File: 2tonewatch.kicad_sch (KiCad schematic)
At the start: 1 part, among them U1 STM32WB55CGUx

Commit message: added eink conn page
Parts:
- removed U1: STM32WB55CGUx, Package_DFN_QFN:QFN-48-1EP_7x7mm_P0.5mm_EP5.6x5.6mm, symbol MCU_ST_STM32WB:STM32WB55CGUx
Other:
- added sheet eink-connector (eink-connector.kicad_sch)

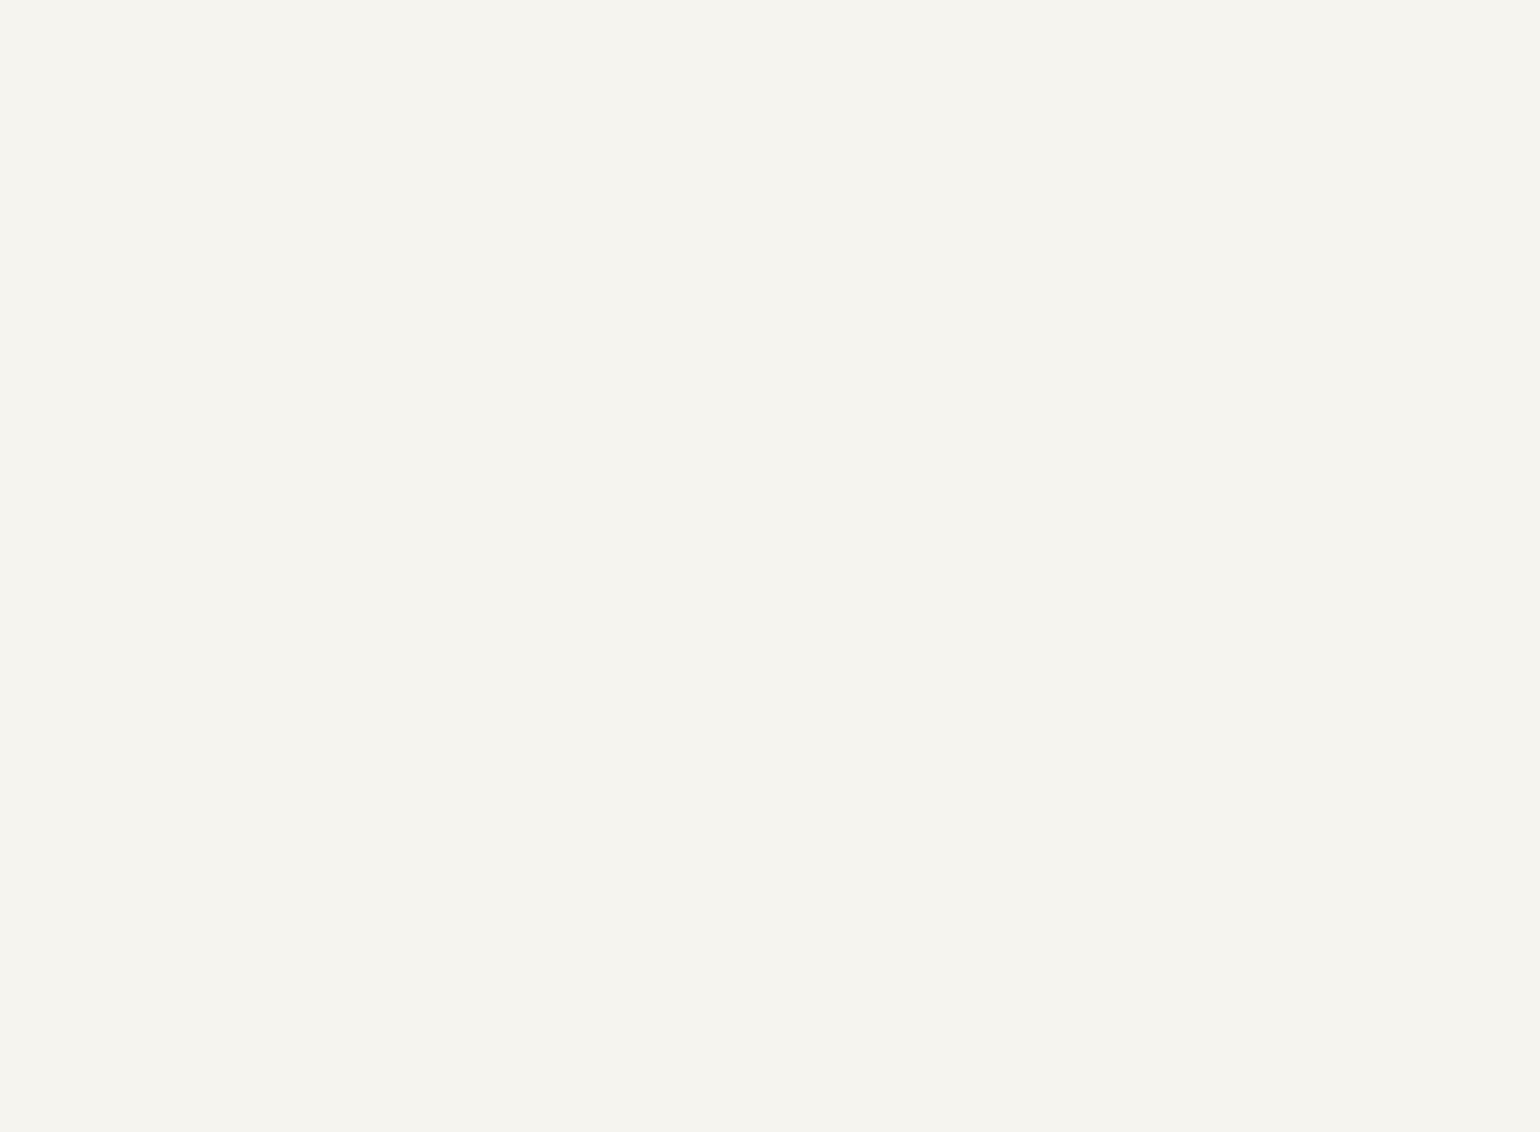
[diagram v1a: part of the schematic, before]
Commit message: Added external flash ic & 4 push buttons
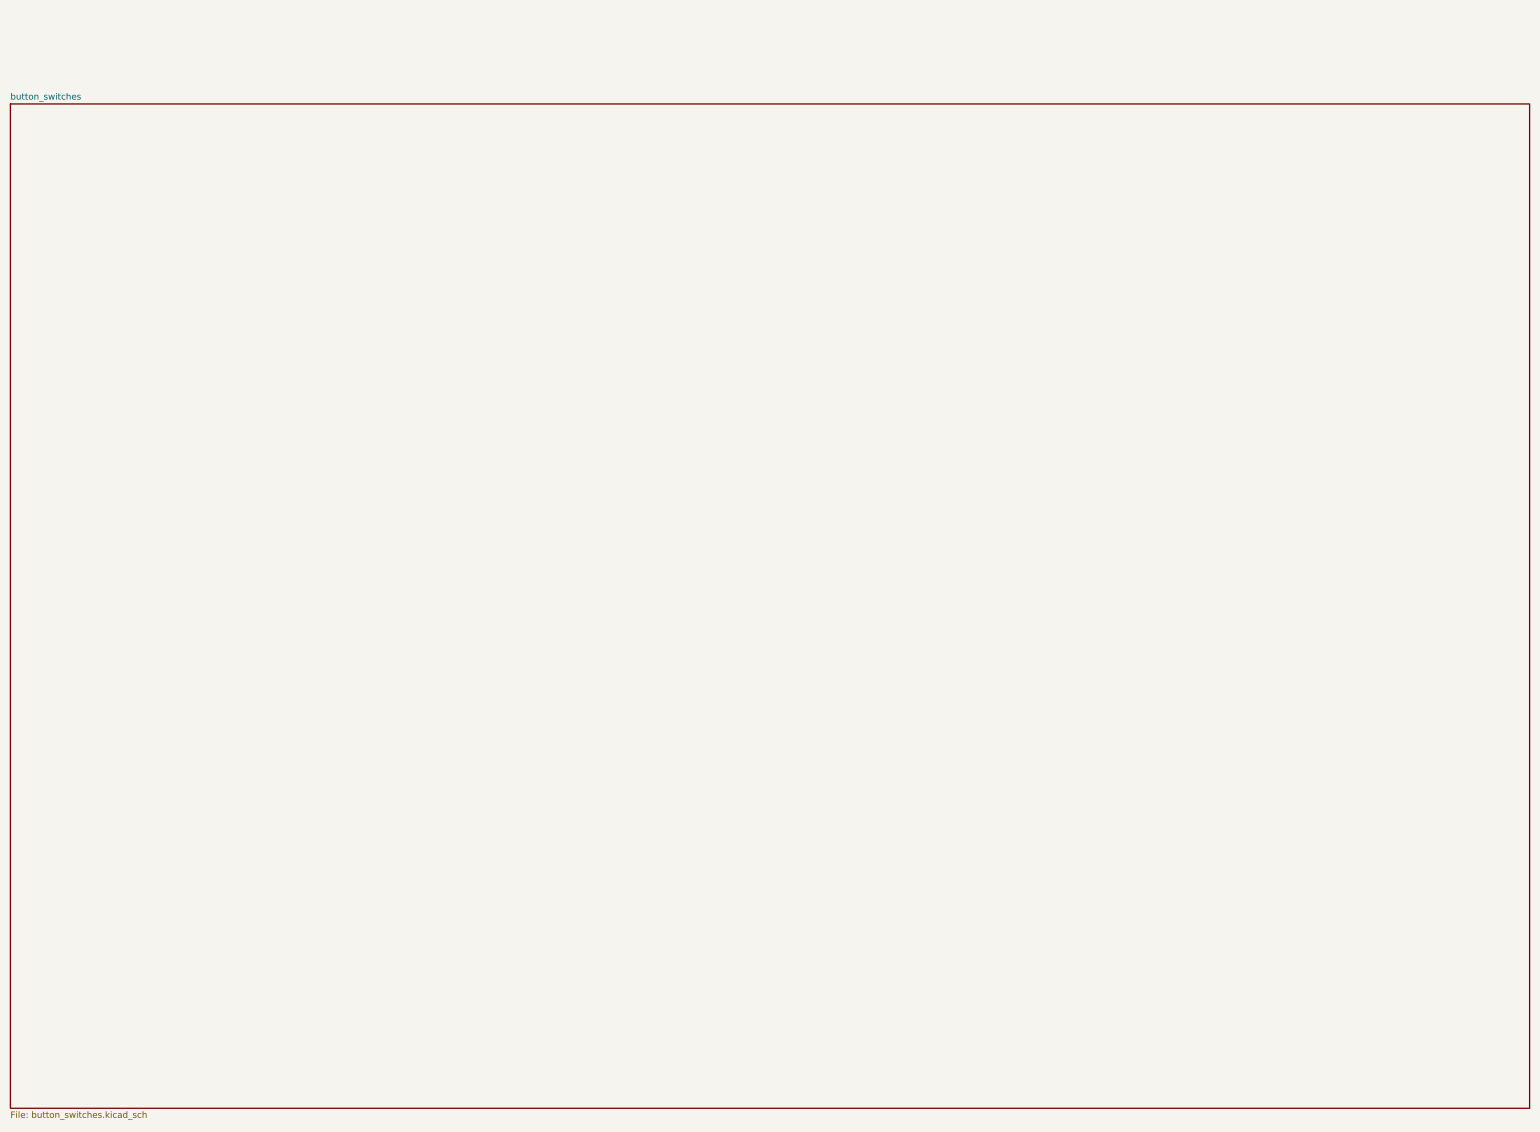
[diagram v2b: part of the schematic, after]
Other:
- added sheet button_switches (button_switches.kicad_sch)
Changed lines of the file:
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@@
 	(paper "A4")
+	(sheet
+		(at -2.54 834.39)
+		(size 303.53 200.66)
+		(exclude_from_sim no)
+		(in_bom yes)
+		(on_board yes)
+		(dnp no)
+		(fields_autoplaced yes)
+		(stroke
+			(width 0.1524)
+			(type solid)
+		)
+		(fill
+			(color 0 0 0 0.0000)
+		)
+		(property "Sheetname" "button_switches"
+			(at -2.54 833.6784 0)
+			(effects
+				(font
+					(size 1.27 1.27)
+				)
+				(justify left bottom)
+			)
+		)
+		(property "Sheetfile" "button_switches.kicad_sch"
+			(at -2.54 1035.6346 0)
+			(effects
+				(font
+					(size 1.27 1.27)
+				)
+				(justify left top)
+			)
+		)
+		(instances
+			(project "2tonewatch"
+				(path "/29eb74dc-e91c-4cc5-ad9f-7f8caf36d690"
+					(page "5")
+				)
+			)
+		)
+	)
 	(sheet
 		(at 0 217.17)

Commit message: Added test points and other cleanup
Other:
- title: (none) -> E-Ink Display BLE Watch 
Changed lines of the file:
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@@
 	(generator_version "9.0")
 	(paper "A4")
+	(title_block
+		(title "E-Ink Display BLE Watch ")
+	)
 	(sheet
 		(at -2.54 834.39)
